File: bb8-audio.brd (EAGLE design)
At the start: 120.3 x 67.3 mm, 27 parts, among them IC1 7805L, IC3 74LS125N

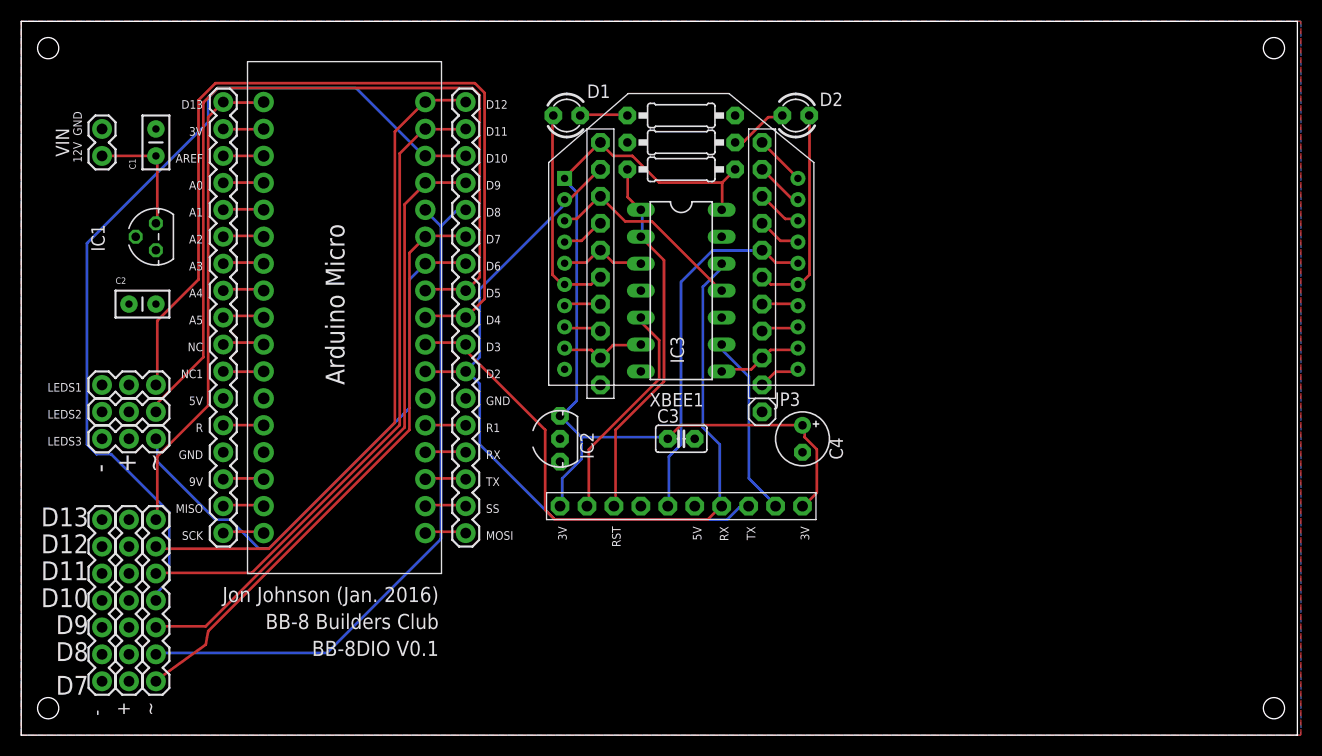
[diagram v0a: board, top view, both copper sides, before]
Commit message: Updated to use Arduino Pro Mini
Updated board and schematic to have an arduino pro mini instead of a
micro.
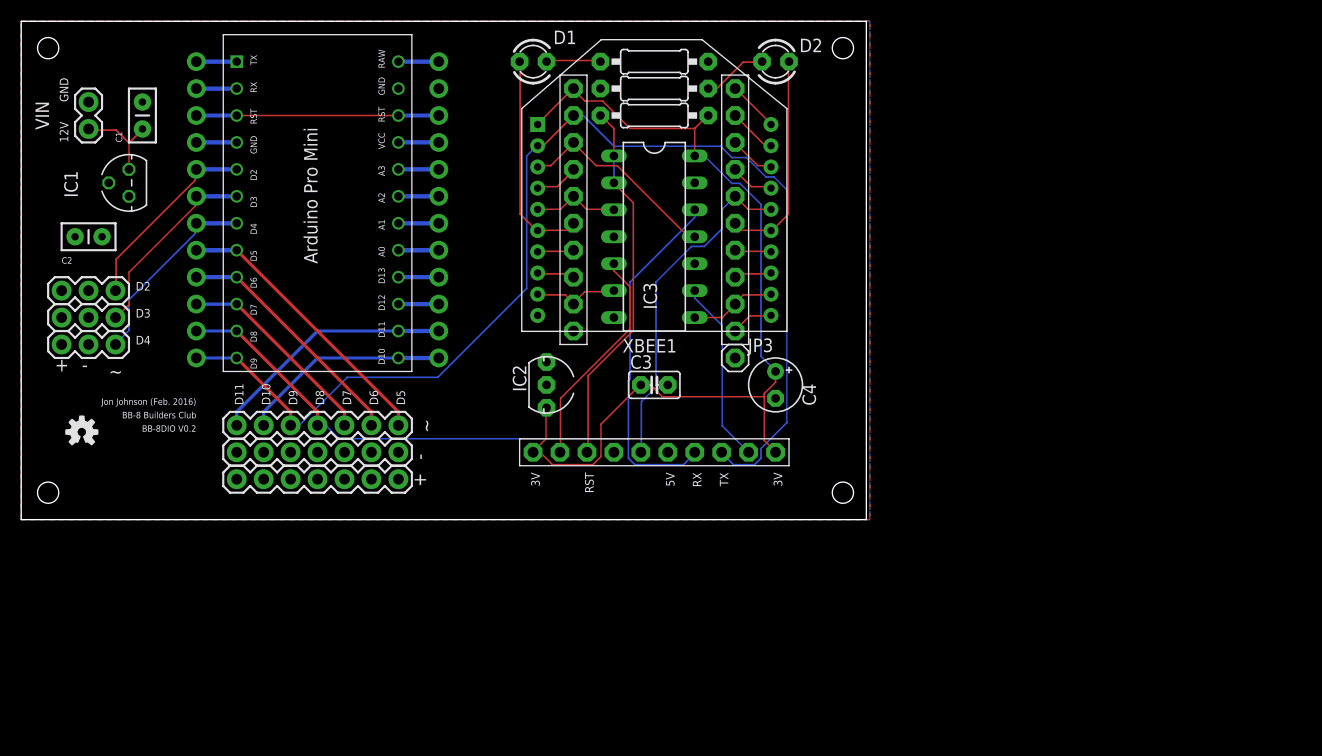
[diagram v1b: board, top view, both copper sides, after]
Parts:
- removed U$3, U$4: M17, SparkFun-Connectors:1X17
- added ARD_PRO_MINI: ARD_PRO_MINI, Arduino-Pro-Mini:ARD_PRO_MINI
- added JP1, JP2: (no value), adafruit:1X12-CB
- U$1: value ARDUINOMICRO -> (none); device adafruit:ARDUINOMICRO -> Spark:OSHW-LOGO-S
- moved ~ 33.2 mm to (33.0, 43.2), turned to 180 degrees
- moved U$1 27.0 mm to (3.17, 42.5), turned to 0 degrees
- moved + 23.9 mm to (17.8, 40.6), turned to 0 degrees
- moved - 22.9 mm to (17.8, 38.1), turned to 0 degrees
- moved LEDS1 9.67 mm to (6.35, 55.9)
- moved LEDS2 9.67 mm to (6.35, 53.3)
- moved LEDS3 9.67 mm to (6.35, 50.8)
- moved C2 8.13 mm to (2.54, 61.0)
- moved D1 5.99 mm to (45.7, 77.5)
- moved R2 5.68 mm to (57.1, 74.9)
- moved C4 5.68 mm to (68.6, 47.0)
- moved IC1 5.68 mm to (7.62, 66.0)
- moved C3 5.68 mm to (57.1, 47.0)
- moved XBEE1 5.68 mm to (57.1, 66.0)
- moved JP3 5.68 mm to (64.8, 49.5)
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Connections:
- removed net 3V: U$1.P$33, U$4.2
- removed net 9V: U$1.P$20, U$4.15
- removed net A4: U$1.P$27, U$4.8
- removed net A5: U$1.P$26, U$4.9
- removed net AREF: U$1.P$32, U$4.3
- removed net MISO: U$1.P$19, U$4.16
- removed net MOSI: U$1.P$17, U$3.1
- removed net NC: U$1.P$25, U$4.10
- removed net NC1: U$1.P$24, U$4.11
- removed net R: U$1.P$13, U$4.13
- removed net R1: U$1.P$22, U$3.5
- removed net SCK: U$1.P$18, U$4.17
- removed net SS: U$1.P$16, U$3.2
- new net RAW: ARD_PRO_MINI.RAW, JP2.1
- new net RST: ARD_PRO_MINI.RST, ARD_PRO_MINI.RST1, JP1.10, JP2.3
- new net VCC: ARD_PRO_MINI.VCC, JP2.4
- net 5V: no longer U$1.P$23, U$4.12
- net A0: now also ARD_PRO_MINI.A0, JP2.8; no longer U$1.P$31, U$4.4
- net A1: now also ARD_PRO_MINI.A1, JP2.7; no longer U$1.P$30, U$4.5
- net A2: now also ARD_PRO_MINI.A2, JP2.6; no longer U$1.P$29, U$4.6
- net A3: now also ARD_PRO_MINI.A3, JP2.5; no longer U$1.P$28, U$4.7
- net D10: now also ARD_PRO_MINI.D10, JP2.12, ~.6; no longer U$1.P$3, U$3.15, ~.4
- net D11: now also ARD_PRO_MINI.D11, JP2.11, ~.7; no longer U$1.P$2, U$3.16, ~.5
- net D12: now also ARD_PRO_MINI.D12, JP2.10; no longer U$1.P$1, U$3.17, ~.6
- net D13: now also ARD_PRO_MINI.D13, JP2.9; no longer U$1.P$34, U$4.1, ~.7
- net D2: now also ARD_PRO_MINI.D2, JP1.8, LEDS1.1; no longer U$1.P$11, U$3.7, U$5.9, U$6.3, XBEE1.2
- net D3: now also ARD_PRO_MINI.D3, JP1.7, LEDS2.1; no longer IC3.12, U$1.P$10, U$3.8, U$6.4
- net D4: now also ARD_PRO_MINI.D4, JP1.6, LEDS3.1; no longer LEDS1.1, U$1.P$9, U$3.9
- net D5: now also ARD_PRO_MINI.D5, JP1.5, ~.1; no longer LEDS2.1, U$1.P$8, U$3.10
- net D6: now also ARD_PRO_MINI.D6, JP1.4, ~.2; no longer LEDS3.1, U$1.P$7, U$3.11
- net D7: now also ARD_PRO_MINI.D7, JP1.3, ~.3; no longer U$1.P$6, U$3.12, ~.1
- net D8: now also ARD_PRO_MINI.D8, IC3.12, JP1.2, U$6.4, ~.4; no longer U$1.P$5, U$3.13, ~.2
- net D9: now also ARD_PRO_MINI.D9, JP1.1, U$5.9, U$6.3, XBEE1.2, ~.5; no longer U$1.P$4, U$3.14, ~.3
- net GND: now also ARD_PRO_MINI.GND, ARD_PRO_MINI.GND1, JP1.9, JP2.2; no longer U$1.P$12, U$1.P$21, U$3.6, U$4.14
- net RX: now also ARD_PRO_MINI.RX, JP1.11; no longer U$1.P$14, U$3.4
- net TX: now also ARD_PRO_MINI.TX, JP1.12; no longer U$1.P$15, U$3.3
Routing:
- net D10: track 84.0 -> 19.9 mm
- net D4: track 82.5 -> 18.4 mm
- net D12: track 63.1 -> 3.81 mm
- net D5: track 80.9 -> 26.6 mm
- net D9: track 58.9 -> 112.2 mm
- net D2: track 64.7 -> 18.4 mm
- net D3: track 64.7 -> 18.5 mm
- net D13: track 45.9 -> 3.81 mm
- net D11: track 61.6 -> 23.5 mm
- net D7: track 56.7 -> 19.4 mm
- net D6: track 53.0 -> 23.0 mm
- net RST: track 0.00 -> 22.9 mm
- net D8: track 66.0 -> 78.7 mm
- net GND: track 0.00 -> 3.97 mm
- net MOSI: track 3.96 -> 0.00 mm
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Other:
- board size 120.3 x 67.3 mm -> 79.7 x 47 mm
- board text added: "BB-8DIO V0.2"
- board text added: "Jon Johnson (Feb. 2016)"
- board text removed: "9V"
- board text removed: "A0"
- board text removed: "A1"
- board text removed: "A2"
- board text removed: "A3"
- board text removed: "A4"
- board text removed: "A5"
- board text removed: "AREF"
- board text removed: "Arduino Micro"
- board text removed: "BB-8DIO V0.1"
- board text removed: "D12"
- board text removed: "D13"
- board text removed: "Jon Johnson (Jan. 2016)"
- board text removed: "LEDS1"
- board text removed: "LEDS2"
- board text removed: "LEDS3"
- board text removed: "MISO"
- board text removed: "MOSI"
- board text removed: "NC"
- board text removed: "NC1"
- board text removed: "R"
- board text removed: "R1"
- board text removed: "SCK"
- board text removed: "SS"
